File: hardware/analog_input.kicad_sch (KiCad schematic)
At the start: 16 parts

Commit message: Add the Cube project
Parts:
- removed C?: 10n, Capacitor_SMD:C_0603_1608Metric_Pad1.08x0.95mm_HandSolder, symbol Device:C_Small
- removed D1: SD24_SOD323, Diode_SMD:D_SOD-323_HandSoldering, symbol Diode:SD24_SOD323
- removed R? (x2): 10k, Resistor_SMD:R_0603_1608Metric_Pad0.98x0.95mm_HandSolder, symbol Device:R_Small
- removed RV?: 1k, Potentiometer_SMD:Potentiometer_Bourns_3214J_Horizontal, symbol Device:R_Potentiometer_Small
- added D12: 5V, symbol Device:D_TVS
- U?: footprint Package_DFN_QFN:TDFN-8-1EP_3x2mm_P0.5mm_EP1.3x1.4mm -> Package_DFN_QFN:TDFN-8-1EP_3x2mm_P0.5mm_EP1.80x1.65mm
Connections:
- net GND: now also D12.1 (A1)
- net IN: now also D12.2 (A2)
- net REF: now reaches U?.2 (-)
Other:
- company: (none) -> Author: I. Kajdan
- moved on the sheet: C?, R?, U?

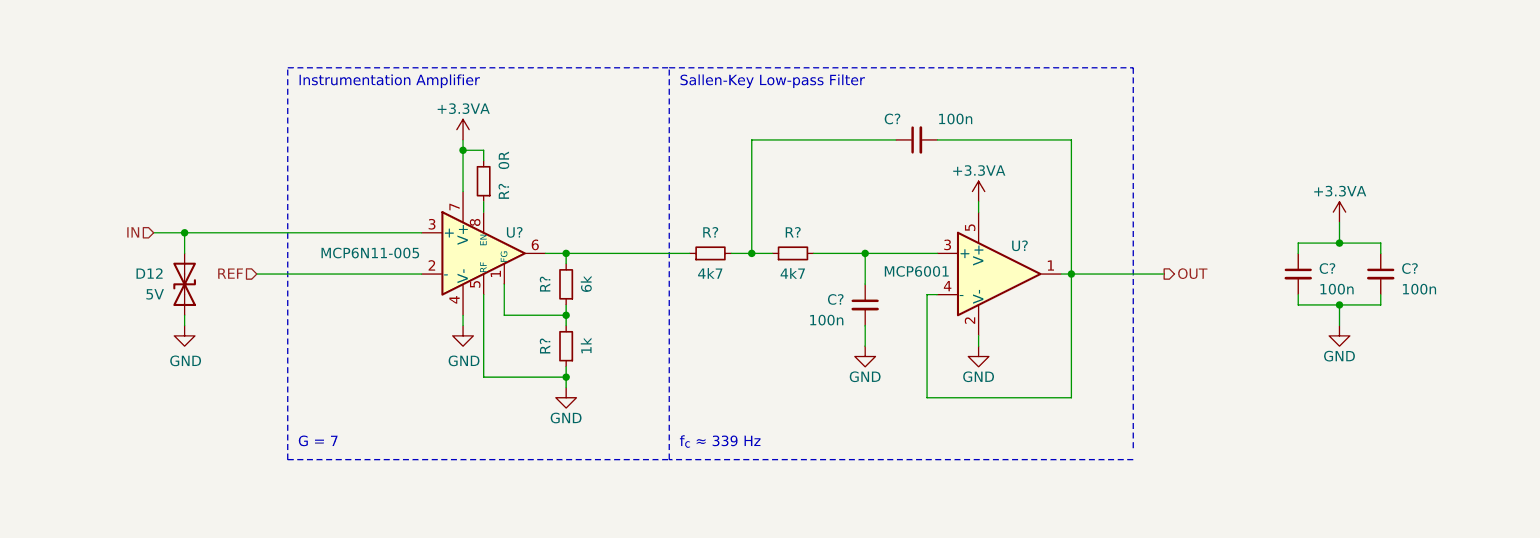
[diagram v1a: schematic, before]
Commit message: Improve the schematic
- add anti-aliasing filters
- rearrange the main connector signals
- improve the power filtering
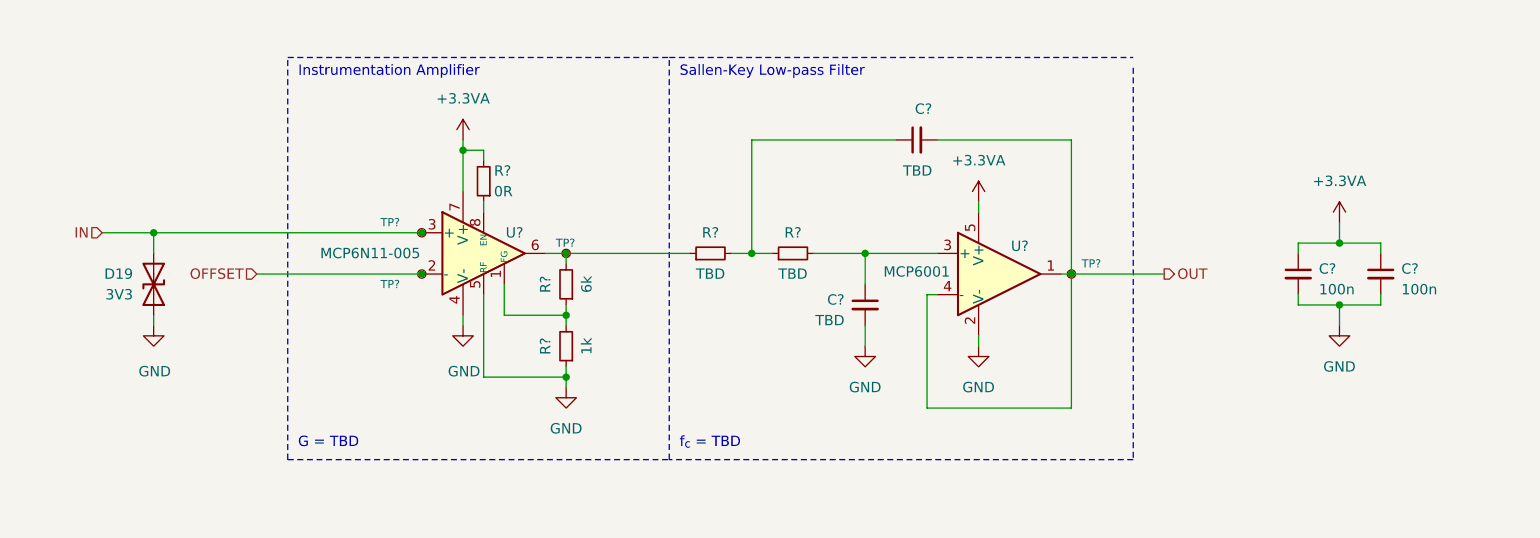
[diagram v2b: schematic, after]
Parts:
- added TP? (x4): TestPoint_Small, TestPoint:TestPoint_Pad_D1.0mm, symbol Connector:TestPoint_Small
- C? (x2): value 100n -> TBD; footprint Capacitor_SMD:C_0603_1608Metric_Pad1.08x0.95mm_HandSolder -> Capacitor_SMD:C_0603_1608Metric
- C? (x2): footprint Capacitor_SMD:C_0603_1608Metric_Pad1.08x0.95mm_HandSolder -> Capacitor_SMD:C_0603_1608Metric
- D19: renamed from D12; value 5V -> 3V3
- R? (x3): footprint Resistor_SMD:R_0603_1608Metric_Pad0.98x0.95mm_HandSolder -> Resistor_SMD:R_0603_1608Metric
- R? (x2): value 4k7 -> TBD; footprint Resistor_SMD:R_0603_1608Metric_Pad0.98x0.95mm_HandSolder -> Resistor_SMD:R_0603_1608Metric
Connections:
- net IN: now also TP?.1
- net OUT: now also TP?.1
- net at R?.1, R?.2, U?.6: now also TP?.1
- net REF renamed OFFSET
- net OFFSET: now also TP?.1
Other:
- note added: "G = TBD"
- note added: "f_{c} = TBD"
- note removed: "G = 7"
- note removed: "f_{c} ≈ 339 Hz"
- moved on the sheet: D19

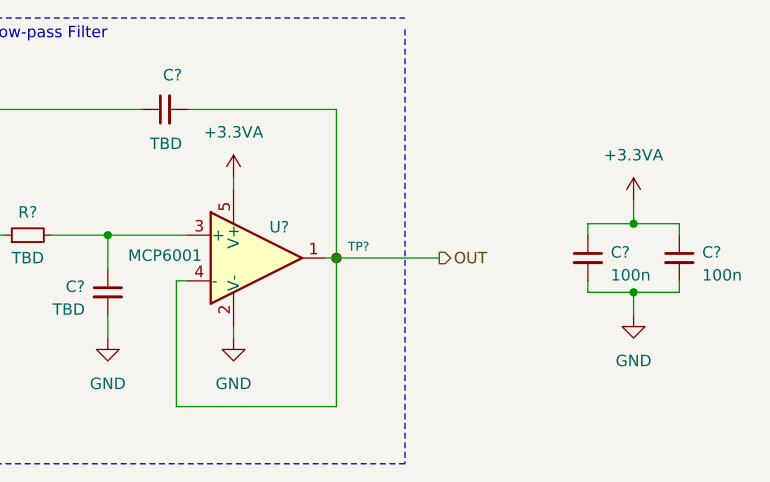
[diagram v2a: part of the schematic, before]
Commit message: Set component values
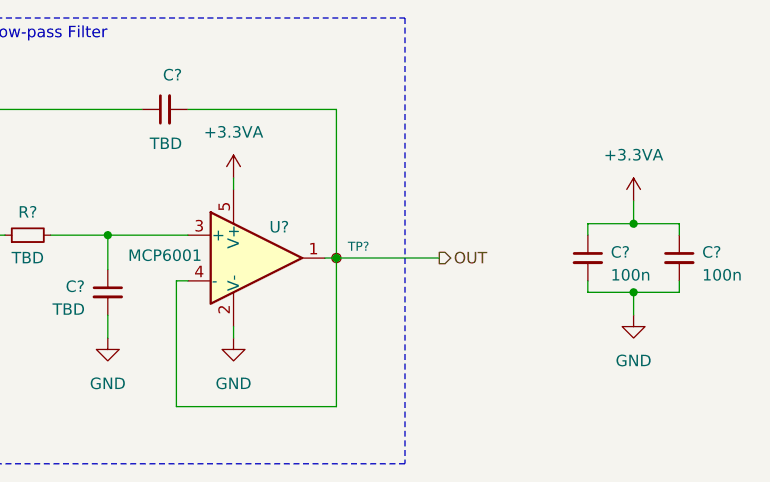
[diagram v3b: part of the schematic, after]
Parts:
- U?: value MCP6N11-005 -> MCP6N11-005

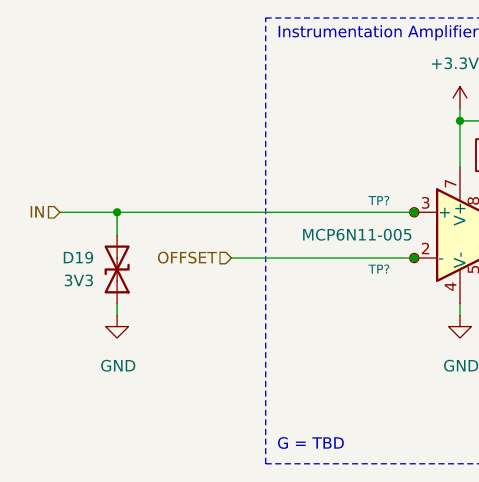
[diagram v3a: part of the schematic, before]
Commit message: Improve the schematic according to the feedback
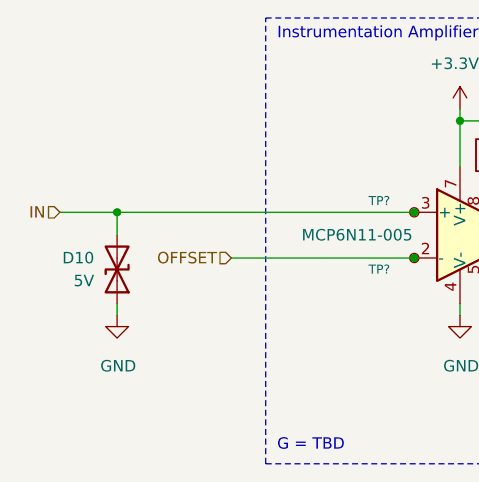
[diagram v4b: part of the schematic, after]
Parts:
- D10: renamed from D19; value 3V3 -> 5V

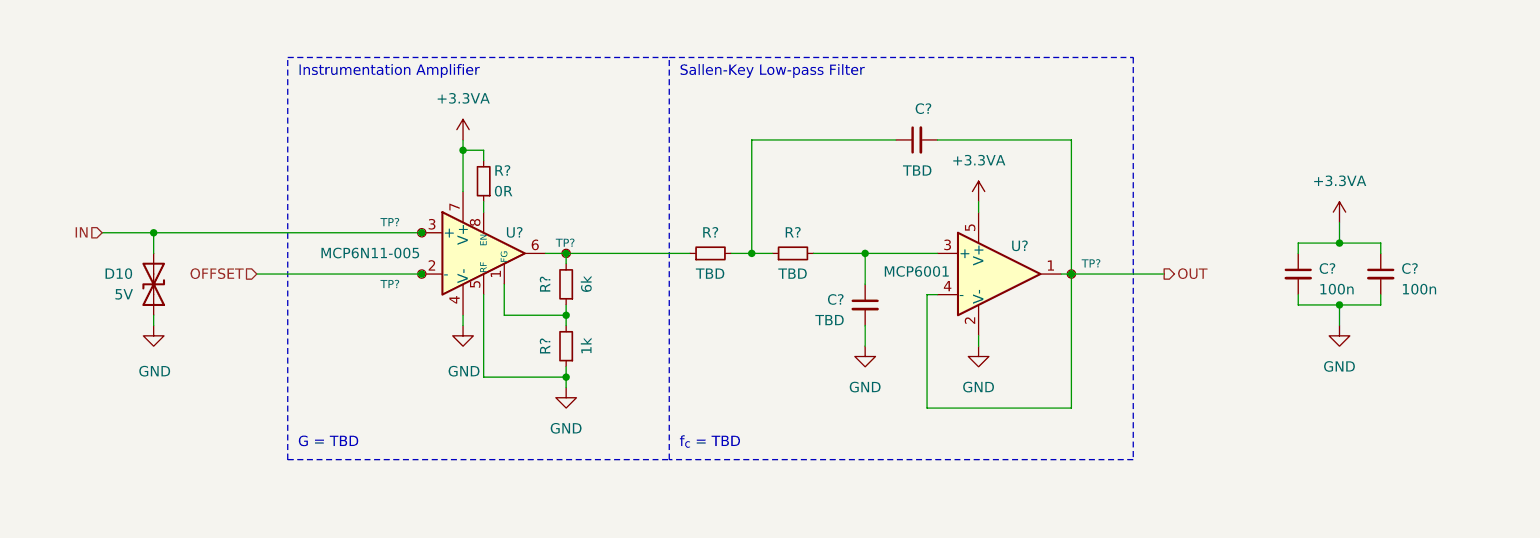
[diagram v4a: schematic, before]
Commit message: Add high-side drivers to the fans and pumps
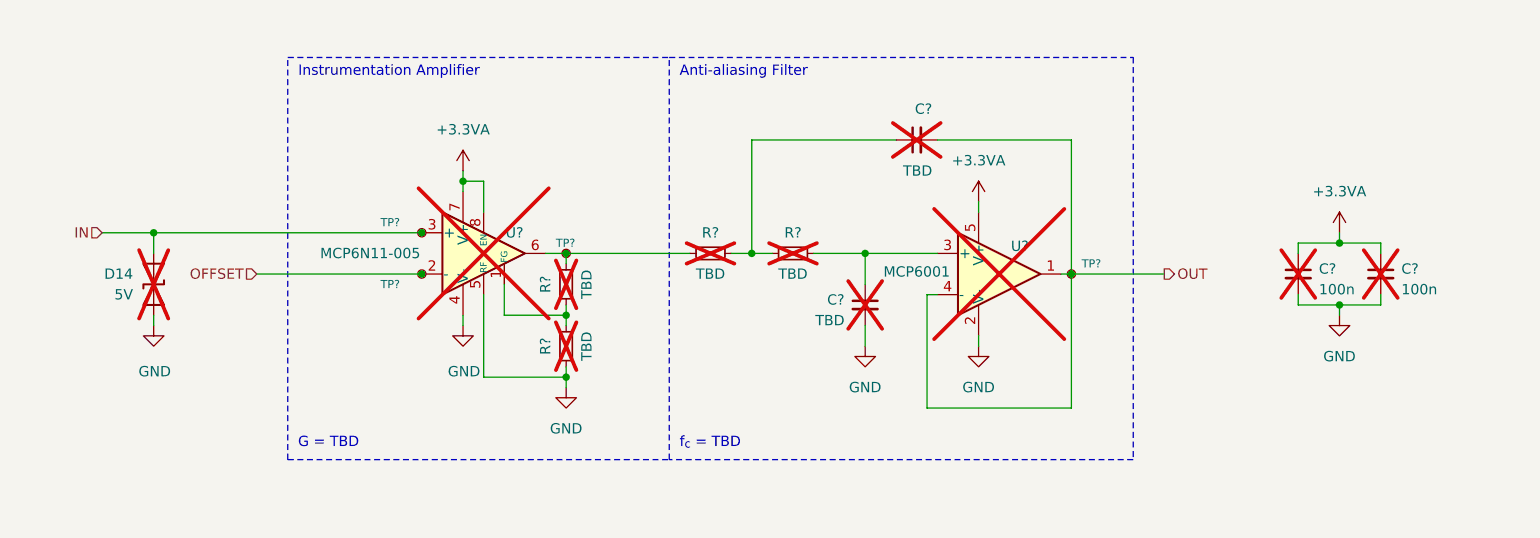
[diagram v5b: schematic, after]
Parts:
- removed R?: 0R, Resistor_SMD:R_0603_1608Metric, symbol Device:R_Small
- C? (x4), R? (x2), U? (x2): now not fitted
- D14: renamed from D10; now not fitted
- R?: value 6k -> TBD; now not fitted
- R?: value 1k -> TBD; now not fitted
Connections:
- net +3.3VA: now also U?.8 (EN)
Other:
- note added: "Anti-aliasing Filter"
- note removed: "Sallen-Key Low-pass Filter"

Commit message: Improve the diagram based on the feedback
- add an input LC filter
- remove the USB connector
- add a programmer connector
- move optocouplers into a subsheet
- add a suspension tension meter IC
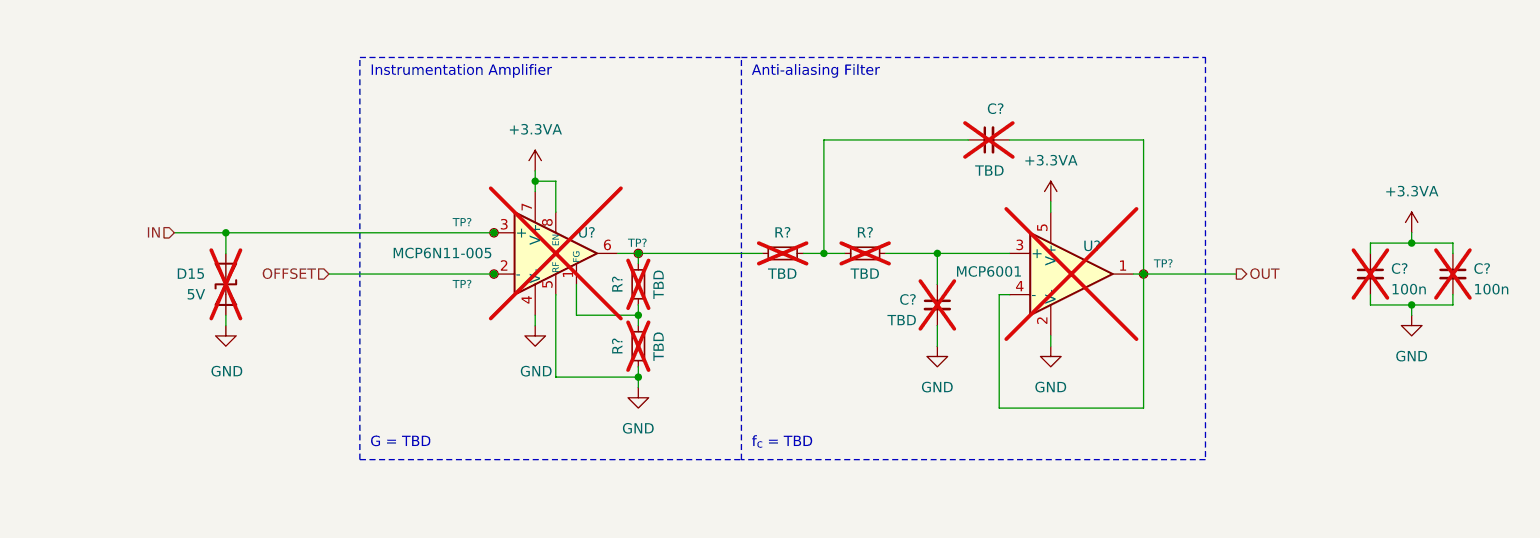
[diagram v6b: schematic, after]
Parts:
- C? (x4), R? (x4), U? (x2): now left out of the parts list
- D15: renamed from D14; footprint (none) -> Diode_SMD:D_SOD-523; Component (none) -> PESD5V0V1BB-QX; now left out of the parts list
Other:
- title: (none) -> Analog Input
- moved on the sheet: C?, D15, R?, TP?, U?
